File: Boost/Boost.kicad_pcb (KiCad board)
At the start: 2 copper layers, 21 parts, among them P1 CONN_01X02, P2 TST, P3 TST, P4 CONN_01X02, U1 TSP61087

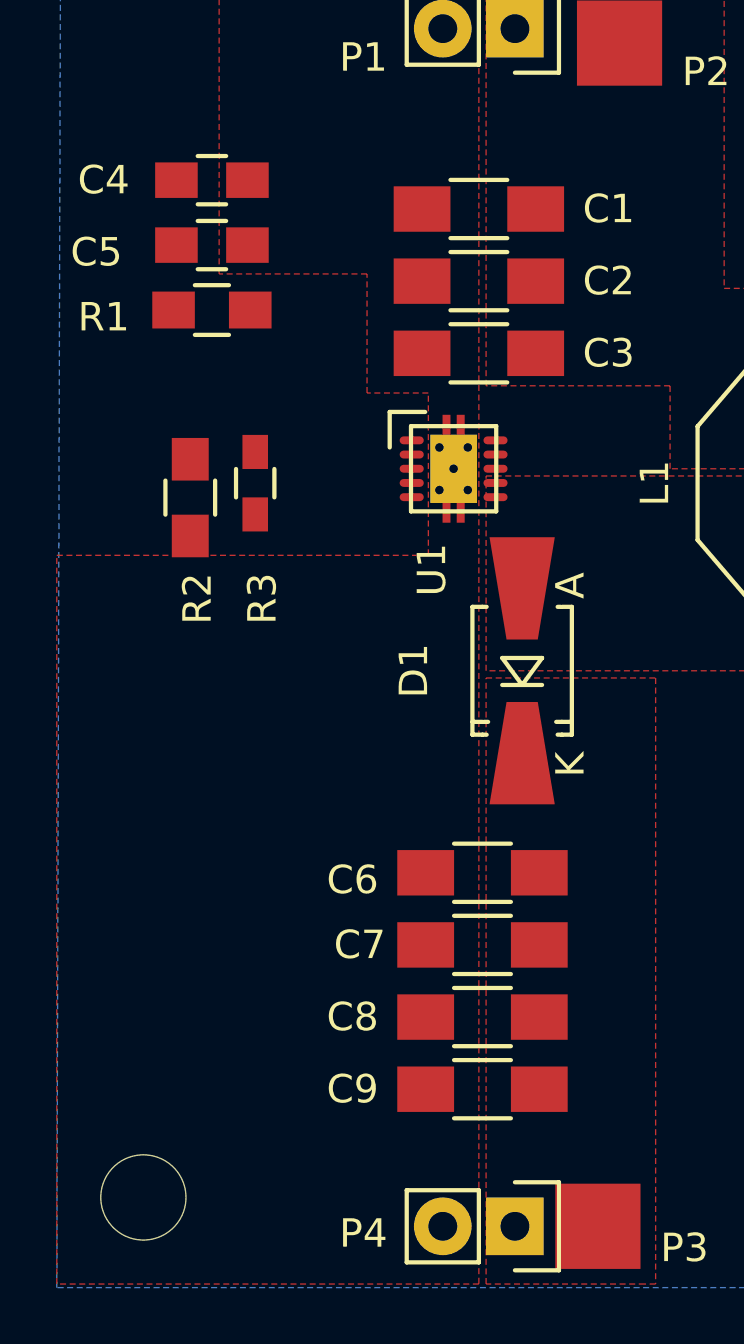
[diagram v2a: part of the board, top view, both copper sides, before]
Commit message: Added routing to the layout
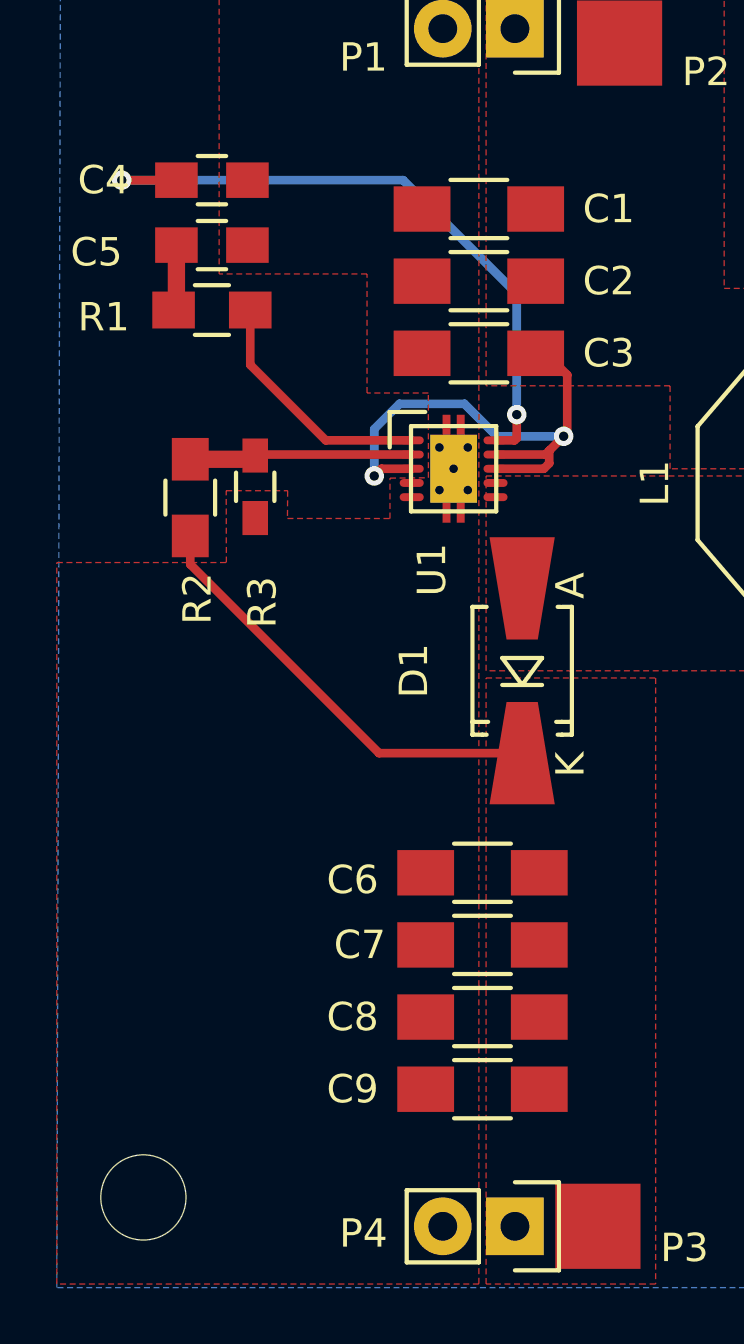
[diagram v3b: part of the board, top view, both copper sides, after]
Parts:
- moved R3 0.13 mm to (151.6, 103.0)
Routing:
- net /SS: track 0.00 -> 23.3 mm, vias 0 -> 2
- net /Lin: track 0.00 -> 19.3 mm, vias 0 -> 2
- net /Vout: track 0.00 -> 15.4 mm
- net /Comp: track 0.00 -> 8.71 mm
- net /FB: track 0.00 -> 7.92 mm
- net Net-(C5-Pad1): track 0.00 -> 2.33 mm
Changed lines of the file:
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@@
   (general
     (links 46)
-    (no_connects 12)
-    (area 144.653 81.807266 179.1394 134.092733)
+    (no_connects 0)
+    (area 141.260074 81.807266 182.940446 134.092733)
     (thickness 1.6)
     (drawings 0)
-    (tracks 0)
+    (tracks 40)
     (zones 0)
     (modules 21)
@@
   )
   (module Resistors_SMD:R_0603_HandSoldering (layer F.Cu)
-    (at 151.638 102.87 270)
+    (at 151.638 102.997 270)
     (descr "Resistor SMD 0603, hand soldering")
     (tags "resistor 0603")
@@
     (pad 1 thru_hole circle (at 0 0) (size 3 3) (drill 3) (layers))
   )
+  (segment (start 157.148 102.362) (end 156.083 102.362) (width 0.3048) (layer F.Cu) (net 1) (status 400000))
+  (via (at 162.4965 101.219) (size 0.6858) (drill 0.3302) (layers F.Cu B.Cu) (net 1))
+  (segment (start 160.147 101.219) (end 162.4965 101.219) (width 0.3048) (layer B.Cu) (net 1))
+  (segment (start 159.004 100.076) (end 160.147 101.219) (width 0.3048) (layer B.Cu) (net 1))
+  (segment (start 156.718 100.076) (end 159.004 100.076) (width 0.3048) (layer B.Cu) (net 1))
+  (segment (start 155.829 100.965) (end 156.718 100.076) (width 0.3048) (layer B.Cu) (net 1))
+  (segment (start 155.829 102.616) (end 155.829 100.965) (width 0.3048) (layer B.Cu) (net 1))
+  (via (at 155.829 102.616) (size 0.6858) (drill 0.3302) (layers F.Cu B.Cu) (net 1))
+  (segment (start 156.083 102.362) (end 155.829 102.616) (width 0.3048) (layer F.Cu) (net 1))
+  (segment (start 160.098 102.362) (end 161.798 102.362) (width 0.3048) (layer F.Cu) (net 1) (status 400000))
+  (segment (start 161.9885 102.1715) (end 161.9885 101.727) (width 0.3048) (layer F.Cu) (net 1))
+  (segment (start 161.798 102.362) (end 161.9885 102.1715) (width 0.3048) (layer F.Cu) (net 1))
+  (segment (start 161.512 98.298) (end 161.8615 98.298) (width 0.3048) (layer F.Cu) (net 1) (status C00000))
+  (segment (start 161.8615 98.298) (end 162.6235 99.06) (width 0.3048) (layer F.Cu) (net 1) (status 400000))
+  (segment (start 162.6235 99.06) (end 162.6235 101.092) (width 0.3048) (layer F.Cu) (net 1))
+  (segment (start 162.6235 101.092) (end 162.4965 101.219) (width 0.3048) (layer F.Cu) (net 1))
+  (segment (start 162.4965 101.219) (end 161.9885 101.727) (width 0.3048) (layer F.Cu) (net 1))
+  (segment (start 161.9885 101.727) (end 161.8535 101.862) (width 0.3048) (layer F.Cu) (net 1))
+  (segment (start 161.8535 101.862) (end 160.098 101.862) (width 0.3048) (layer F.Cu) (net 1) (status 800000))
+  (segment (start 160.098 101.362) (end 160.766 101.362) (width 0.3048) (layer F.Cu) (net 3) (status 400000))
+  (segment (start 146.939 92.202) (end 148.864 92.202) (width 0.3048) (layer F.Cu) (net 3) (status 800000))
+  (via (at 146.939 92.202) (size 0.6858) (drill 0.3302) (layers F.Cu B.Cu) (net 3))
+  (segment (start 156.845 92.202) (end 146.939 92.202) (width 0.3048) (layer B.Cu) (net 3))
+  (segment (start 160.8455 96.2025) (end 156.845 92.202) (width 0.3048) (layer B.Cu) (net 3))
+  (segment (start 160.8455 100.457) (end 160.8455 96.2025) (width 0.3048) (layer B.Cu) (net 3))
+  (via (at 160.8455 100.457) (size 0.6858) (drill 0.3302) (layers F.Cu B.Cu) (net 3))
+  (segment (start 160.8455 101.2825) (end 160.8455 100.457) (width 0.3048) (layer F.Cu) (net 3))
+  (segment (start 160.766 101.362) (end 160.8455 101.2825) (width 0.3048) (layer F.Cu) (net 3))
+  (segment (start 148.864 94.488) (end 148.864 96.674) (width 0.6096) (layer F.Cu) (net 4) (status C00000))
+  (segment (start 148.864 96.674) (end 148.764 96.774) (width 0.6096) (layer F.Cu) (net 4) (status C00000))
+  (segment (start 149.352 104.728) (end 149.352 105.7275) (width 0.3048) (layer F.Cu) (net 5) (status 400000))
+  (segment (start 155.99918 112.37468) (end 161.036 112.37468) (width 0.3048) (layer F.Cu) (net 5) (status 800000))
+  (segment (start 149.352 105.7275) (end 155.99918 112.37468) (width 0.3048) (layer F.Cu) (net 5))
+  (segment (start 157.148 101.362) (end 154.12288 101.362) (width 0.3048) (layer F.Cu) (net 7) (status 400000))
+  (segment (start 151.464 98.70312) (end 151.464 96.774) (width 0.3048) (layer F.Cu) (net 7) (status 800000))
+  (segment (start 154.12288 101.362) (end 151.464 98.70312) (width 0.3048) (layer F.Cu) (net 7))
+  (segment (start 157.148 101.862) (end 151.673 101.862) (width 0.3048) (layer F.Cu) (net 8) (status C00000))
+  (segment (start 151.673 101.862) (end 151.638 101.897) (width 0.3048) (layer F.Cu) (net 8) (status C00000))
+  (segment (start 149.352 102.028) (end 151.38 102.028) (width 0.6096) (layer F.Cu) (net 8))
+  (segment (start 151.38 102.028) (end 151.638 101.77) (width 0.6096) (layer F.Cu) (net 8))
   (zone (net 5) (net_name /Vout) (layer F.Cu) (hatch edge 0.508)
     (connect_pads yes (clearance 0.1524))
@@
     (polygon
       (pts
-        (xy 159.512 131.064) (xy 144.653 131.064) (xy 144.653 105.41) (xy 157.734 105.41) (xy 157.734 99.695)
-        (xy 155.575 99.695) (xy 155.575 95.504) (xy 150.368 95.504) (xy 150.368 85.217) (xy 159.512 85.217)
-        (xy 159.512 131.064)
+        (xy 159.512 131.064) (xy 144.653 131.064) (xy 144.653 105.664) (xy 150.622 105.664) (xy 150.61692 103.13416)
+        (xy 152.779705 103.134933) (xy 152.77338 104.11206) (xy 156.38272 104.1146) (xy 156.38272 102.6922) (xy 157.735132 102.679483)
+        (xy 157.734 99.695) (xy 155.575 99.695) (xy 155.575 95.504) (xy 150.368 95.504) (xy 150.368 85.217)
+        (xy 159.512 85.217) (xy 159.512 131.064)
       )
     )

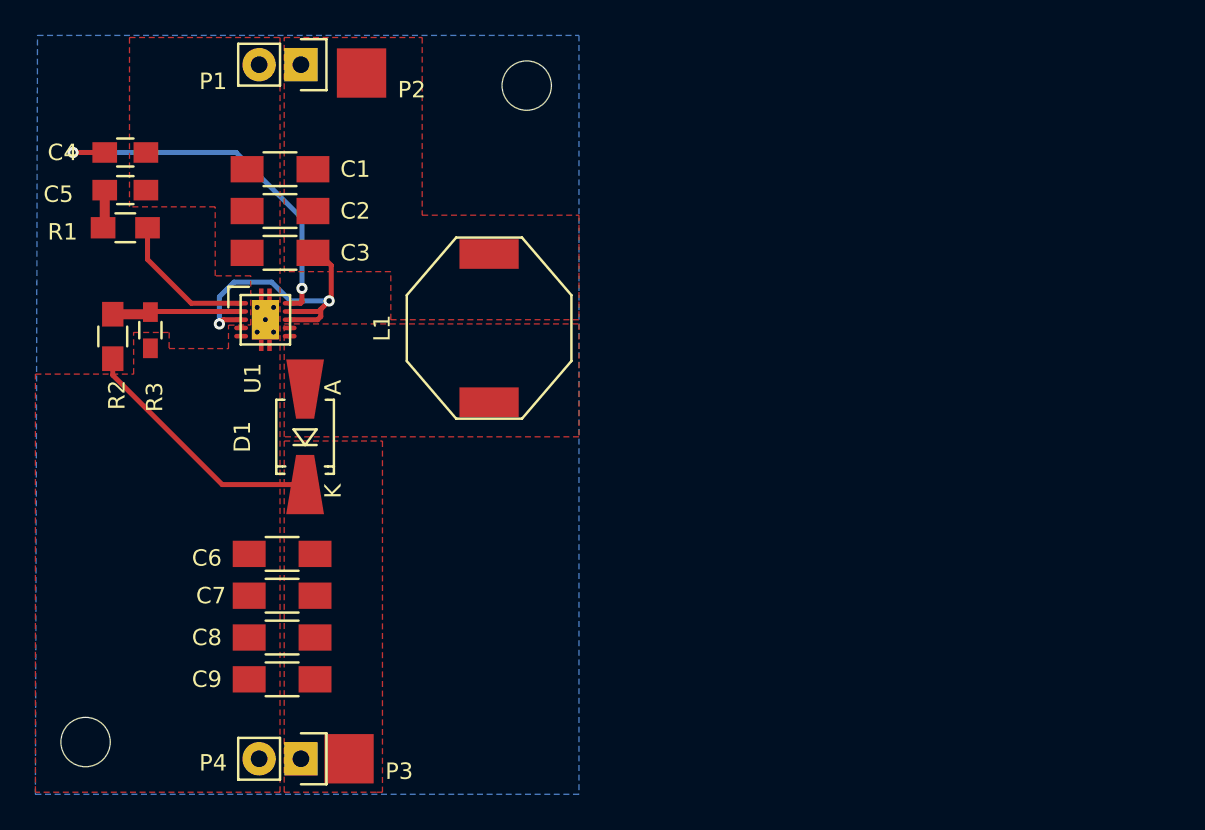
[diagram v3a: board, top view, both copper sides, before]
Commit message: Added stitching and labels
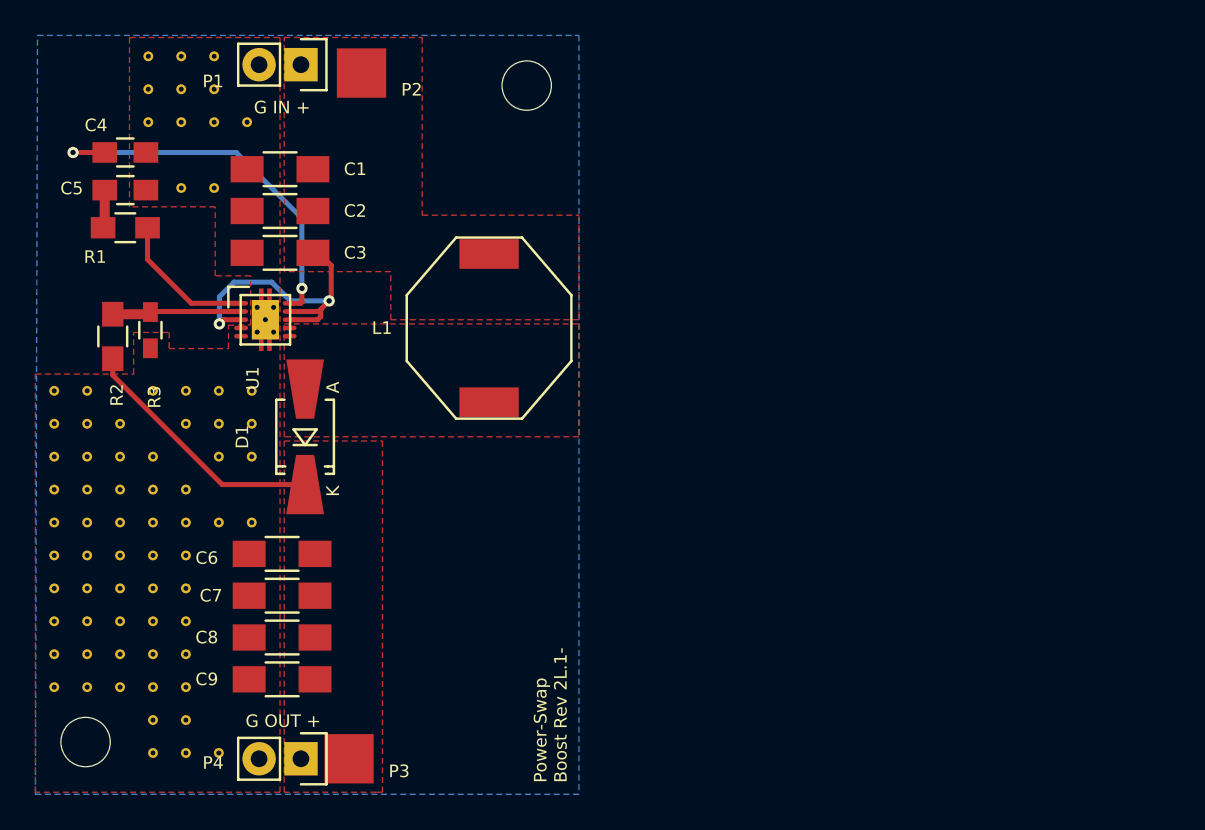
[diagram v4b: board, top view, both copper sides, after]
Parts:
- added REF**1211: VIA-0.6mm, Boost-Footprints:VIA-0.6mm, F.Cu at (151.5, 86.4)
- added REF**121111: VIA-0.6mm, Boost-Footprints:VIA-0.6mm, F.Cu at (145.8, 106.7)
- added REF**1211110: VIA-0.6mm, Boost-Footprints:VIA-0.6mm, F.Cu at (145.8, 124.7)
- added REF**121112: VIA-0.6mm, Boost-Footprints:VIA-0.6mm, F.Cu at (145.8, 108.7)
- added REF**121113: VIA-0.6mm, Boost-Footprints:VIA-0.6mm, F.Cu at (145.8, 110.7)
- added REF**121114: VIA-0.6mm, Boost-Footprints:VIA-0.6mm, F.Cu at (145.8, 112.7)
- added REF**121115: VIA-0.6mm, Boost-Footprints:VIA-0.6mm, F.Cu at (145.8, 114.7)
- added REF**121116: VIA-0.6mm, Boost-Footprints:VIA-0.6mm, F.Cu at (145.8, 116.7)
- added REF**121117: VIA-0.6mm, Boost-Footprints:VIA-0.6mm, F.Cu at (145.8, 118.7)
- added REF**121118: VIA-0.6mm, Boost-Footprints:VIA-0.6mm, F.Cu at (145.8, 120.7)
- added REF**121119: VIA-0.6mm, Boost-Footprints:VIA-0.6mm, F.Cu at (145.8, 122.7)
- added REF**121121: VIA-0.6mm, Boost-Footprints:VIA-0.6mm, F.Cu at (147.8, 106.7)
- added REF**1211210: VIA-0.6mm, Boost-Footprints:VIA-0.6mm, F.Cu at (147.8, 124.7)
- added REF**121122: VIA-0.6mm, Boost-Footprints:VIA-0.6mm, F.Cu at (147.8, 108.7)
- added REF**121123: VIA-0.6mm, Boost-Footprints:VIA-0.6mm, F.Cu at (147.8, 110.7)
- added REF**121124: VIA-0.6mm, Boost-Footprints:VIA-0.6mm, F.Cu at (147.8, 112.7)
- added REF**121125: VIA-0.6mm, Boost-Footprints:VIA-0.6mm, F.Cu at (147.8, 114.7)
- added REF**121126: VIA-0.6mm, Boost-Footprints:VIA-0.6mm, F.Cu at (147.8, 116.7)
- added REF**121127: VIA-0.6mm, Boost-Footprints:VIA-0.6mm, F.Cu at (147.8, 118.7)
- added REF**121128: VIA-0.6mm, Boost-Footprints:VIA-0.6mm, F.Cu at (147.8, 120.7)
- added REF**121129: VIA-0.6mm, Boost-Footprints:VIA-0.6mm, F.Cu at (147.8, 122.7)
- added REF**1211310: VIA-0.6mm, Boost-Footprints:VIA-0.6mm, F.Cu at (149.8, 124.7)
- added REF**121132: VIA-0.6mm, Boost-Footprints:VIA-0.6mm, F.Cu at (149.8, 108.7)
- added REF**121133: VIA-0.6mm, Boost-Footprints:VIA-0.6mm, F.Cu at (149.8, 110.7)
- added REF**121134: VIA-0.6mm, Boost-Footprints:VIA-0.6mm, F.Cu at (149.8, 112.7)
- added REF**121135: VIA-0.6mm, Boost-Footprints:VIA-0.6mm, F.Cu at (149.8, 114.7)
- added REF**121136: VIA-0.6mm, Boost-Footprints:VIA-0.6mm, F.Cu at (149.8, 116.7)
- added REF**121137: VIA-0.6mm, Boost-Footprints:VIA-0.6mm, F.Cu at (149.8, 118.7)
- added REF**121138: VIA-0.6mm, Boost-Footprints:VIA-0.6mm, F.Cu at (149.8, 120.7)
- added REF**121139: VIA-0.6mm, Boost-Footprints:VIA-0.6mm, F.Cu at (149.8, 122.7)
- added REF**121141: VIA-0.6mm, Boost-Footprints:VIA-0.6mm, F.Cu at (151.8, 106.7)
- added REF**1211410: VIA-0.6mm, Boost-Footprints:VIA-0.6mm, F.Cu at (151.8, 124.7)
- added REF**1211411: VIA-0.6mm, Boost-Footprints:VIA-0.6mm, F.Cu at (151.8, 126.7)
- added REF**1211412: VIA-0.6mm, Boost-Footprints:VIA-0.6mm, F.Cu at (151.8, 128.7)
- added REF**121143: VIA-0.6mm, Boost-Footprints:VIA-0.6mm, F.Cu at (151.8, 110.7)
- added REF**121144: VIA-0.6mm, Boost-Footprints:VIA-0.6mm, F.Cu at (151.8, 112.7)
- added REF**121145: VIA-0.6mm, Boost-Footprints:VIA-0.6mm, F.Cu at (151.8, 114.7)
- added REF**121146: VIA-0.6mm, Boost-Footprints:VIA-0.6mm, F.Cu at (151.8, 116.7)
- added REF**121147: VIA-0.6mm, Boost-Footprints:VIA-0.6mm, F.Cu at (151.8, 118.7)
- added REF**121148: VIA-0.6mm, Boost-Footprints:VIA-0.6mm, F.Cu at (151.8, 120.7)
- added REF**121149: VIA-0.6mm, Boost-Footprints:VIA-0.6mm, F.Cu at (151.8, 122.7)
- added REF**121151: VIA-0.6mm, Boost-Footprints:VIA-0.6mm, F.Cu at (153.8, 106.7)
- added REF**1211510: VIA-0.6mm, Boost-Footprints:VIA-0.6mm, F.Cu at (153.8, 124.7)
- added REF**1211511: VIA-0.6mm, Boost-Footprints:VIA-0.6mm, F.Cu at (153.8, 126.7)
- added REF**1211512: VIA-0.6mm, Boost-Footprints:VIA-0.6mm, F.Cu at (153.8, 128.7)
- added REF**121152: VIA-0.6mm, Boost-Footprints:VIA-0.6mm, F.Cu at (153.8, 108.7)
- added REF**121154: VIA-0.6mm, Boost-Footprints:VIA-0.6mm, F.Cu at (153.8, 112.7)
- added REF**121155: VIA-0.6mm, Boost-Footprints:VIA-0.6mm, F.Cu at (153.8, 114.7)
- added REF**121156: VIA-0.6mm, Boost-Footprints:VIA-0.6mm, F.Cu at (153.8, 116.7)
- added REF**121157: VIA-0.6mm, Boost-Footprints:VIA-0.6mm, F.Cu at (153.8, 118.7)
- added REF**121158: VIA-0.6mm, Boost-Footprints:VIA-0.6mm, F.Cu at (153.8, 120.7)
- added REF**121159: VIA-0.6mm, Boost-Footprints:VIA-0.6mm, F.Cu at (153.8, 122.7)
- added REF**121161: VIA-0.6mm, Boost-Footprints:VIA-0.6mm, F.Cu at (155.8, 106.7)
- added REF**1211612: VIA-0.6mm, Boost-Footprints:VIA-0.6mm, F.Cu at (155.8, 128.7)
- added REF**121162: VIA-0.6mm, Boost-Footprints:VIA-0.6mm, F.Cu at (155.8, 108.7)
- added REF**121163: VIA-0.6mm, Boost-Footprints:VIA-0.6mm, F.Cu at (155.8, 110.7)
- added REF**121165: VIA-0.6mm, Boost-Footprints:VIA-0.6mm, F.Cu at (155.8, 114.7)
- added REF**121171: VIA-0.6mm, Boost-Footprints:VIA-0.6mm, F.Cu at (157.8, 106.7)
- added REF**121172: VIA-0.6mm, Boost-Footprints:VIA-0.6mm, F.Cu at (157.8, 108.7)
- added REF**121173: VIA-0.6mm, Boost-Footprints:VIA-0.6mm, F.Cu at (157.8, 110.7)
- added REF**121175: VIA-0.6mm, Boost-Footprints:VIA-0.6mm, F.Cu at (157.8, 114.7)
- added REF**1212: VIA-0.6mm, Boost-Footprints:VIA-0.6mm, F.Cu at (151.5, 88.4)
- added REF**1213: VIA-0.6mm, Boost-Footprints:VIA-0.6mm, F.Cu at (151.5, 90.4)
- added REF**1221: VIA-0.6mm, Boost-Footprints:VIA-0.6mm, F.Cu at (153.5, 86.4)
- added REF**1222: VIA-0.6mm, Boost-Footprints:VIA-0.6mm, F.Cu at (153.5, 88.4)
- added REF**1223: VIA-0.6mm, Boost-Footprints:VIA-0.6mm, F.Cu at (153.5, 90.4)
- added REF**1225: VIA-0.6mm, Boost-Footprints:VIA-0.6mm, F.Cu at (153.5, 94.4)
- added REF**1231: VIA-0.6mm, Boost-Footprints:VIA-0.6mm, F.Cu at (155.5, 86.4)
- added REF**1232: VIA-0.6mm, Boost-Footprints:VIA-0.6mm, F.Cu at (155.5, 88.4)
- added REF**1233: VIA-0.6mm, Boost-Footprints:VIA-0.6mm, F.Cu at (155.5, 90.4)
- added REF**1235: VIA-0.6mm, Boost-Footprints:VIA-0.6mm, F.Cu at (155.5, 94.4)
- added REF**1243: VIA-0.6mm, Boost-Footprints:VIA-0.6mm, F.Cu at (157.5, 90.4)
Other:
- board text added: "G IN +"
- board text added: "G OUT +"
- board text added: "Power-Swap Boost Rev 2L.1-"

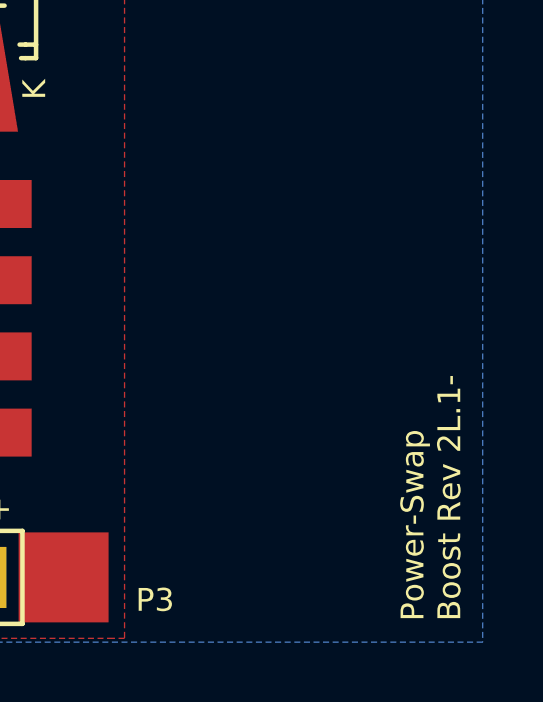
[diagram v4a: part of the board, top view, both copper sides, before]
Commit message: Added the layout diagram and updated the version information on the board
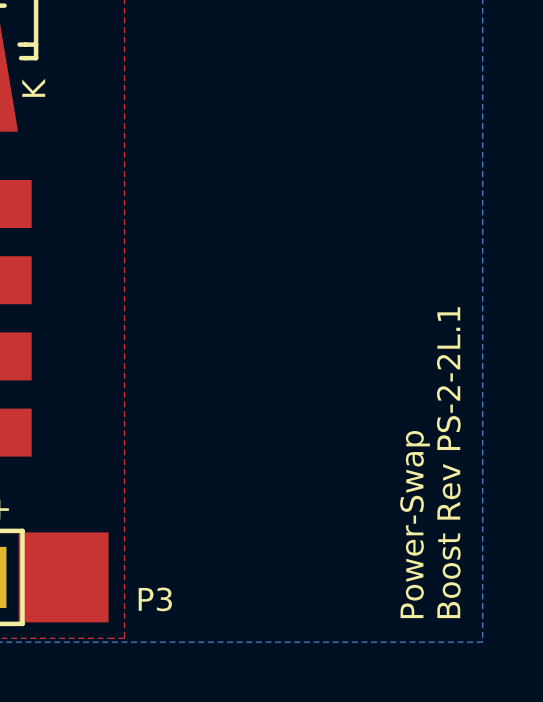
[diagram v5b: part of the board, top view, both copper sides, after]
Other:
- board text added: "Power-Swap Boost Rev PS-2-2L.1"
- board text removed: "Power-Swap Boost Rev 2L.1-"
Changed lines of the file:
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@@
     (links 118)
     (no_connects 0)
-    (area 140.092409 81.807266 182.940446 134.092733)
+    (area 141.407244 82.9691 181.211947 133.76656)
     (thickness 1.6)
     (drawings 3)
@@
   )
   (setup
-    (last_trace_width 0.3048)
+    (last_trace_width 0.1524)
     (user_trace_width 0.3048)
     (user_trace_width 0.6096)
@@
     (effects (font (size 0.762 0.762) (thickness 0.127)))
   )
-  (gr_text "Power-Swap\nBoost Rev 2L.1-" (at 175.9585 130.4925 90) (layer F.SilkS)
+  (gr_text "Power-Swap\nBoost Rev PS-2-2L.1" (at 175.9585 130.4925 90) (layer F.SilkS)
     (effects (font (size 0.762 0.762) (thickness 0.127)) (justify left))
   )
